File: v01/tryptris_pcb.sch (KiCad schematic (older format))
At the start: 70 parts

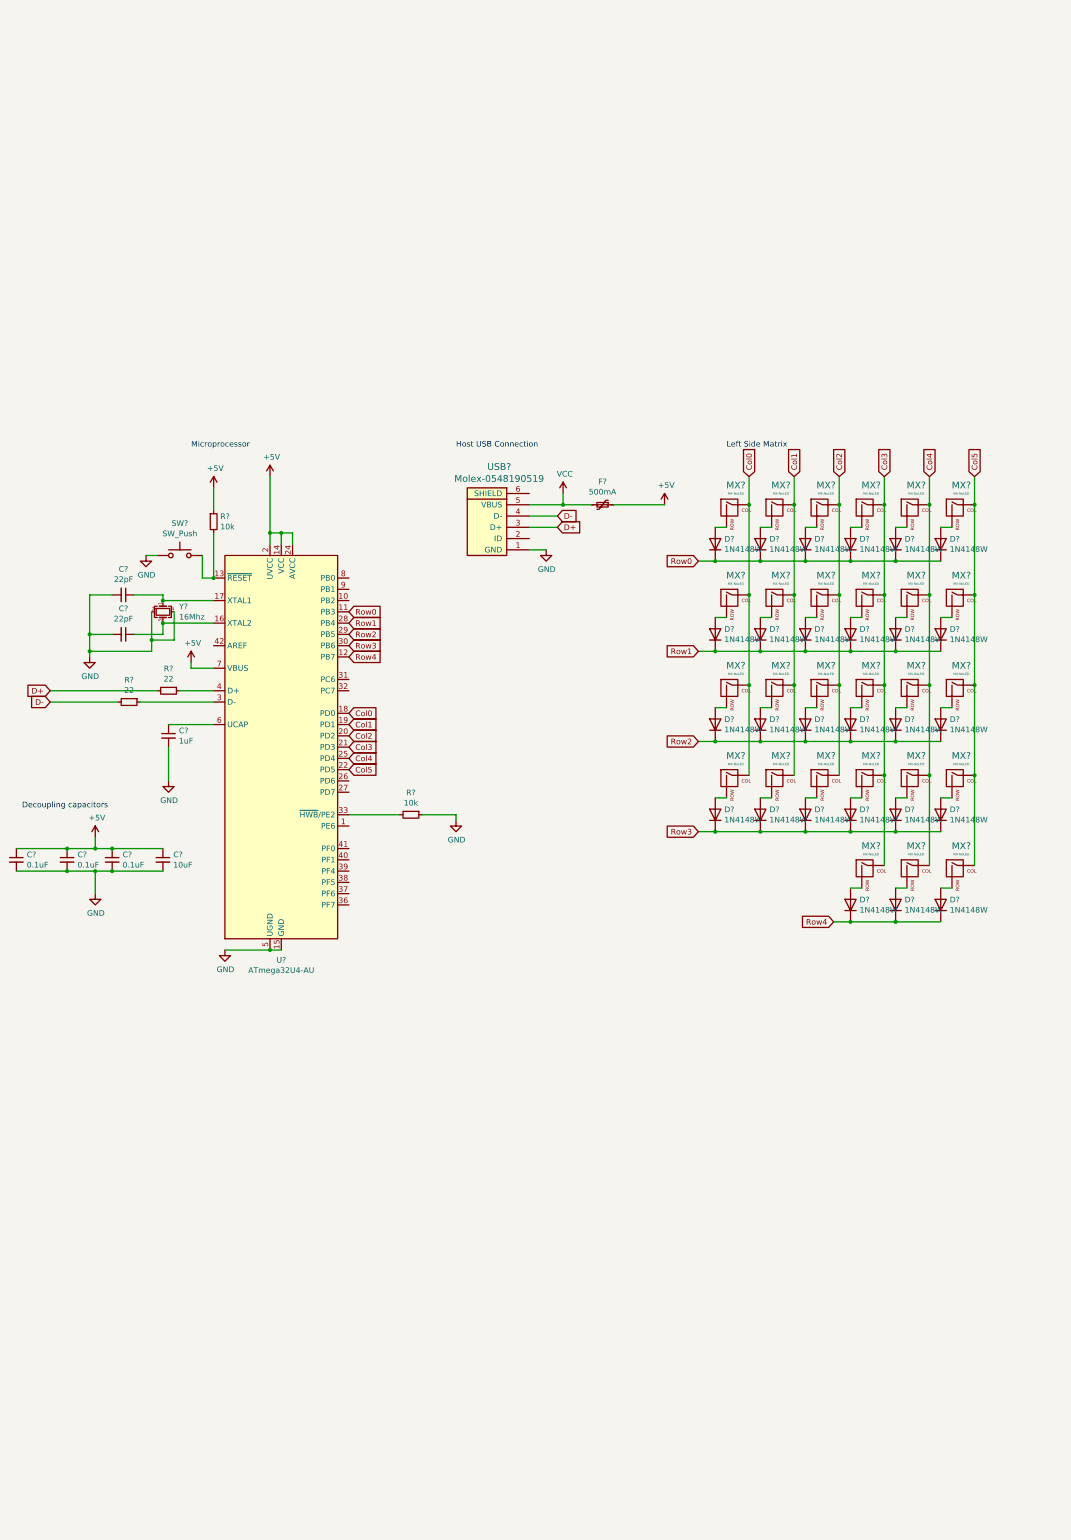
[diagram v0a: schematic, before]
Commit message: Add right side components to schematics
Still need to get a USBC port for the upstream connection.
Not jazzed about using TRRS for the interconnects, but I need to figure
out how USBC ports would work there. TRRS might be simpler given that
this will be a PCB board.
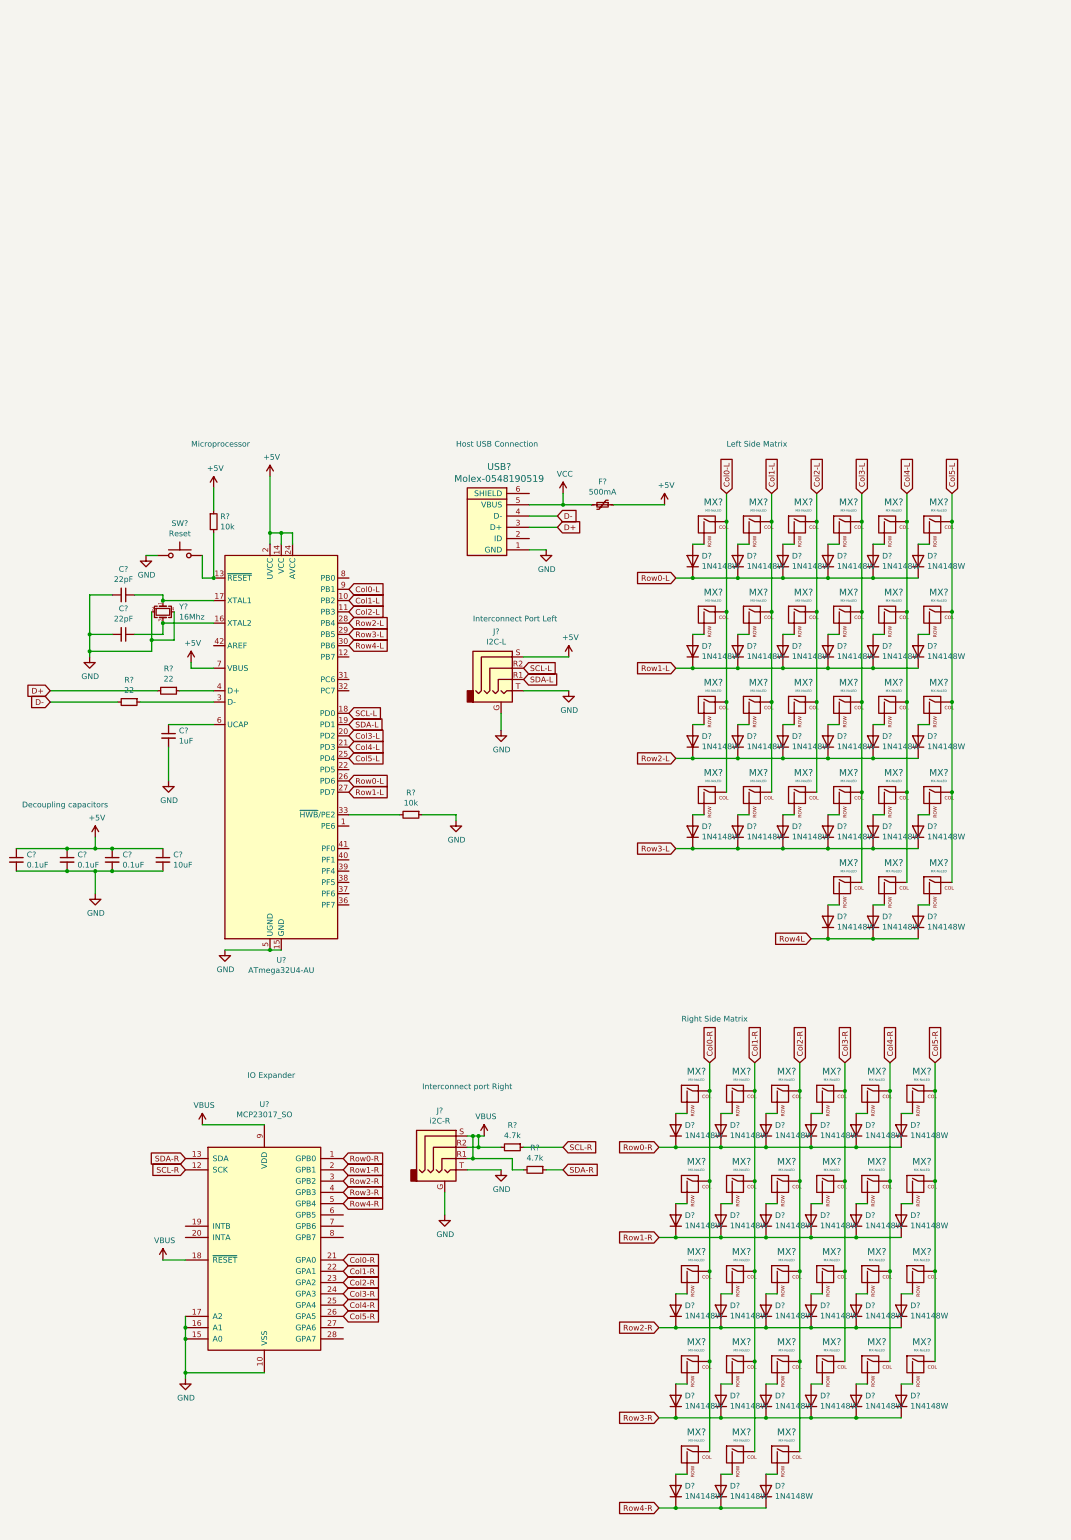
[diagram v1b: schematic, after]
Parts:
- added D? (x27): 1N4148W, Diode_SMD:D_SOD-123, symbol Diode:1N4148W
- added J?: i2C-R, symbol Connector:AudioJack4_Ground
- added J?: I2C-L, symbol Connector:AudioJack4_Ground
- added MX? (x27): MX-NoLED, symbol MX_Alps_Hybrid:MX-NoLED
- added R? (x2): 4.7k, symbol Device:R_Small
- added U?: MCP23017_SO, Package_SO:SOIC-28W_7.5x17.9mm_P1.27mm, symbol Interface_Expansion:MCP23017_SO
- SW?: value SW_Push -> Reset
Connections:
- net +5V: now also J?.S
- net GND: now also J?.G, J?.G, J?.T, J?.T, U?.10 (VSS), U?.15 (A0), U?.16 (A1), U?.17 (A2)
- net Col1-L: now reaches U?.10 (PB2)
- net Col1-L: now also MX?.1 (COL), MX?.1 (COL), MX?.1 (COL), MX?.1 (COL)
- net Row0-L: now reaches U?.26 (PD6)
- net Row0-L: now also D?.1 (K), D?.1 (K), D?.1 (K), D?.1 (K), D?.1 (K), D?.1 (K)
- net Row1-L: now reaches U?.27 (PD7)
- net Row1-L: now also D?.1 (K), D?.1 (K), D?.1 (K), D?.1 (K), D?.1 (K), D?.1 (K)
- net Col0-L: now reaches U?.9 (PB1)
- net Col0-L: now also MX?.1 (COL), MX?.1 (COL), MX?.1 (COL), MX?.1 (COL)
- removed net Col0: MX?.1 (COL), MX?.1 (COL), MX?.1 (COL), MX?.1 (COL), U?.18 (PD0)
- removed net Col1: MX?.1 (COL), MX?.1 (COL), MX?.1 (COL), MX?.1 (COL), U?.19 (PD1)
- net Col2 renamed Col2-L
- net Col2-L: now also U?.11 (PB3); no longer U?.20 (PD2)
- net Col3 renamed Col3-L
- net Col3-L: now also U?.20 (PD2); no longer U?.21 (PD3)
- net Col4 renamed Col4-L
- net Col4-L: now also U?.21 (PD3); no longer U?.25 (PD4)
- net Col5 renamed Col5-L
- net Col5-L: now also U?.25 (PD4); no longer U?.22 (PD5)
- removed net Row0: D?.1 (K), D?.1 (K), D?.1 (K), D?.1 (K), D?.1 (K), D?.1 (K), U?.11 (PB3)
- removed net Row1: D?.1 (K), D?.1 (K), D?.1 (K), D?.1 (K), D?.1 (K), D?.1 (K), U?.28 (PB4)
- net Row2 renamed Row2-L
- net Row2-L: now also U?.28 (PB4); no longer U?.29 (PB5)
- net Row3 renamed Row3-L
- net Row3-L: now also U?.29 (PB5); no longer U?.30 (PB6)
- net Row4 renamed Row4L
- net Row4L: no longer U?.12 (PB7)
- new net: D?.2 (A), MX?.2 (ROW) (x27)
- new net Col0-R: MX?.1 (COL), MX?.1 (COL), MX?.1 (COL), MX?.1 (COL), MX?.1 (COL), U?.21 (GPA0)
- new net Col1-R: MX?.1 (COL), MX?.1 (COL), MX?.1 (COL), MX?.1 (COL), MX?.1 (COL), U?.22 (GPA1)
- new net Col2-R: MX?.1 (COL), MX?.1 (COL), MX?.1 (COL), MX?.1 (COL), MX?.1 (COL), U?.23 (GPA2)
- new net Col3-R: MX?.1 (COL), MX?.1 (COL), MX?.1 (COL), MX?.1 (COL), U?.24 (GPA3)
- new net Col4-R: MX?.1 (COL), MX?.1 (COL), MX?.1 (COL), MX?.1 (COL), U?.25 (GPA4)
- new net Col5-R: MX?.1 (COL), MX?.1 (COL), MX?.1 (COL), MX?.1 (COL), U?.26 (GPA5)
- new net Row0-R: D?.1 (K), D?.1 (K), D?.1 (K), D?.1 (K), D?.1 (K), D?.1 (K), U?.1 (GPB0)
- new net Row1-R: D?.1 (K), D?.1 (K), D?.1 (K), D?.1 (K), D?.1 (K), D?.1 (K), U?.2 (GPB1)
- new net Row2-R: D?.1 (K), D?.1 (K), D?.1 (K), D?.1 (K), D?.1 (K), D?.1 (K), U?.3 (GPB2)
- new net Row3-R: D?.1 (K), D?.1 (K), D?.1 (K), D?.1 (K), D?.1 (K), D?.1 (K), U?.4 (GPB3)
- new net Row4-L: U?.30 (PB6)
- new net Row4-R: D?.1 (K), D?.1 (K), D?.1 (K), U?.5 (GPB4)
- new net SCL-L: J?.R2, U?.18 (PD0)
- new net SCL-R: R?.1, U?.12 (SCK)
- new net SDA-L: J?.R1, U?.19 (PD1)
- new net SDA-R: R?.1, U?.13 (SDA)
- new net VBUS: J?.R1, J?.R2, J?.S, R?.2, R?.2, U?.18 (~RESET~), U?.9 (VDD)
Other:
- note added: "IO Expander"
- note added: "Interconnect Port Left"
- note added: "Interconnect port Right"
- note added: "Right Side Matrix\n"
- moved on the sheet: D?, MX?

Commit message: Revise schematic
* Use a better USB connector schematic and footprint for a through-hole
  connector.
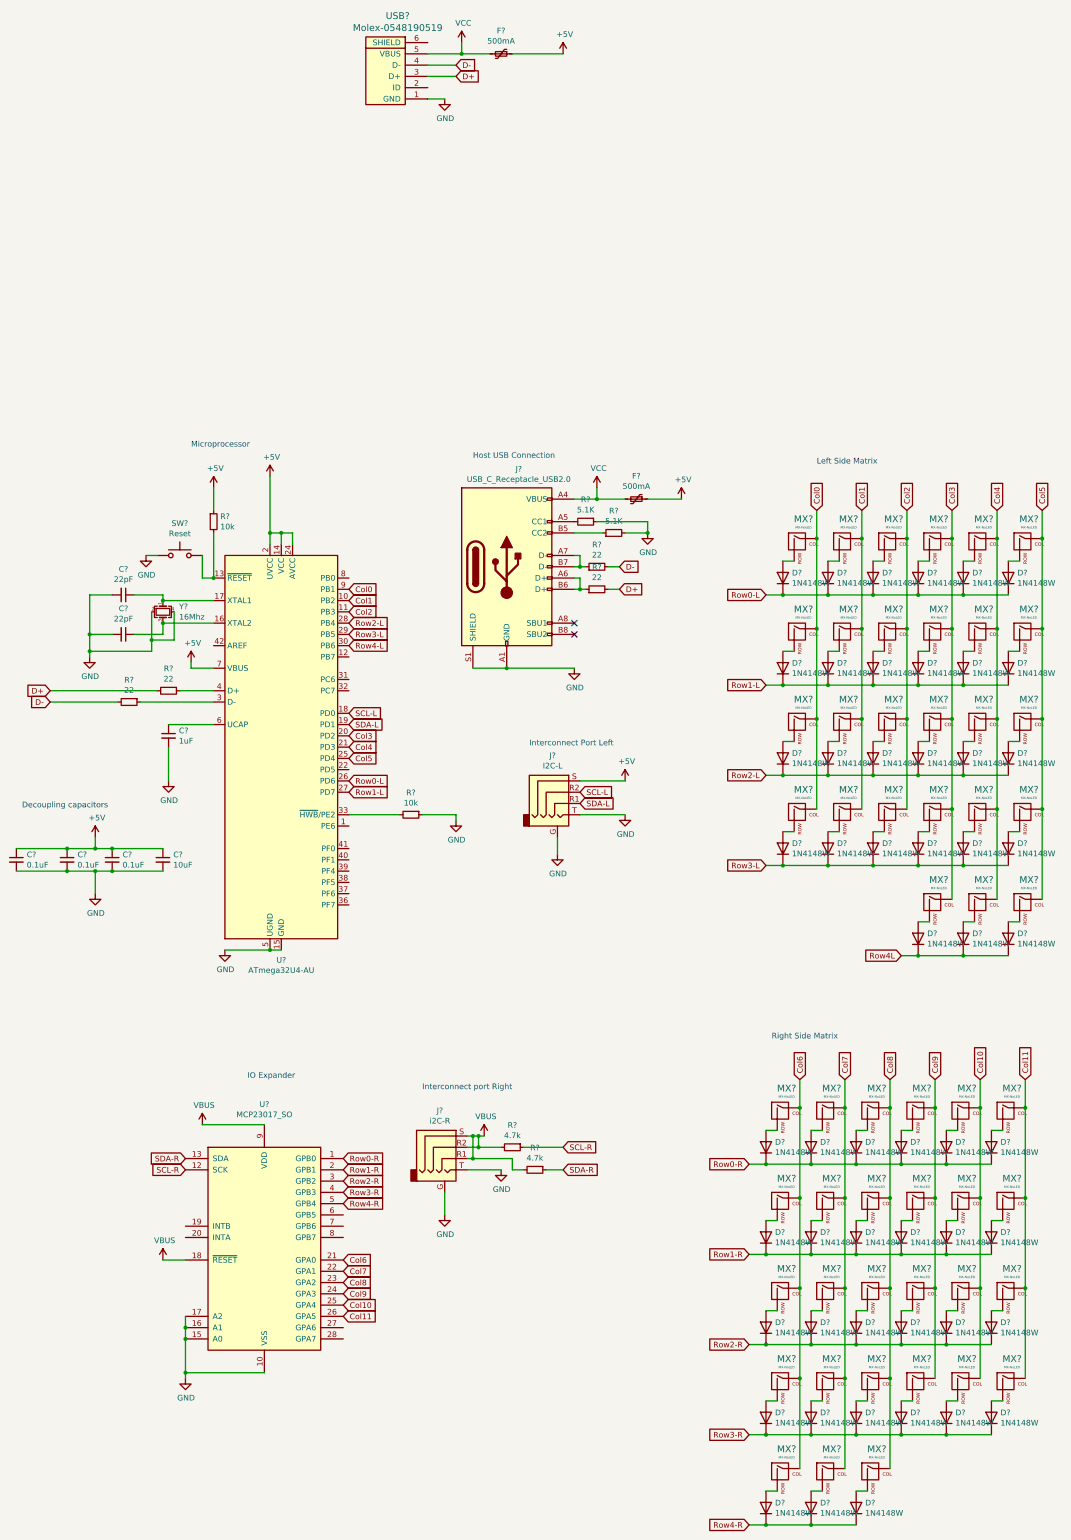
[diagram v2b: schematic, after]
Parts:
- added F?: 500mA, symbol Device:Polyfuse_Small
- added J?: USB_C_Receptacle_USB2.0, symbol Connector:USB_C_Receptacle_USB2.0
- added R? (x2): 5.1K, symbol Device:R_Small
- added R? (x2): 22, symbol Device:R_Small
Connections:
- net +5V: now also F?.1
- net D+: now also R?.2
- net D-: now also R?.2
- net GND: now also J?.A1 (GND), J?.A12 (GND), J?.B1 (GND), J?.B12 (GND), J?.S1 (SHIELD), R?.1, R?.2
- net VCC: now also F?.2, J?.A4 (VBUS), J?.A9 (VBUS), J?.B4 (VBUS), J?.B9 (VBUS)
- net Col0-L renamed Col0
- net Col0-R renamed Col6
- net Col1-L renamed Col1
- net Col1-R renamed Col7
- net Col2-L renamed Col2
- net Col2-R renamed Col8
- net Col3-L renamed Col3
- net Col3-R renamed Col9
- net Col4-L renamed Col4
- net Col4-R renamed Col10
- net Col5-L renamed Col5
- net Col5-R renamed Col11
- new net: J?.A5 (CC1), R?.2
- new net: J?.A6 (D+), J?.B6 (D+), R?.1
- new net: J?.A7 (D-), J?.B7 (D-), R?.1
- new net: J?.B5 (CC2), R?.1
- no-connect marks 0 -> 2
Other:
- moved on the sheet: D?, F?, J?, MX?, USB?
